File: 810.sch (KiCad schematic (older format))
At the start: 307 parts, among them J1 PJ301BM, J10 PJ301BM, J11 PJ301BM, J12 PJ301BM, J13 PJ301BM, J14 PJ301BM, J15 JACK_MONO_SW, J16 PJ301BM, J17 PJ301B, J18 PJ301B, J2 PJ301BM, J3 PJ301BM, J4 PJ301B, J5 PJ301B, J6 PJ301BM, J7 PJ301BM, J8 PJ301BM, J9 PJ301BM, P1 CONN_01X08, P2 CONN_02X05, P3 CONN_01X03, P4 CONN_01X08, P5 CONN_01X02, Q1 PMBT2369, Q10 2SK208-GR, Q11 2SC4738, Q12 2SA1832, Q13 2SA1832, Q14 2SA1832, Q15 2SC4738, Q2 2SK208-GR, Q3 2SA1618, Q4 2SC4207, Q5 2SK208-GR, Q6 MMBF4391LT1G, Q7 2SA1832, Q8 PMBT2369, Q9 2SK208-GR, SW1 SPDT, SW2 SPDT, SW3 BF3-1050, SW4 SPDT, SW5 DP6T-ALPHA-SR2511, U1 TL072-, U10 TL072-, U11 TL072-, U12 TA75S558F, U13 TA75S558F, U14 TA75S558F, U15 TA75S558F, U16 TA75S558F, U17 CD4052, U18 TA75S558F, U2 TL072-, U3 TL072-, U4 CD40106, U5 CD4027, U6 LM13700, U7 LM13700, U8 LM13700, U9 TL072-

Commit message: added secret sub-oscillator
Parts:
- added C20: 47p, MyModules:SM0603-C-JRL, symbol C_US
- added C47, C48: 0.1µ, MyModules:SM0603-C-JRL, symbol C_US
- added D20, D21, D22: 1N4148, MyModules:SOD323-C1A2, symbol D
- added P6: CONN_02X03, Pin_Headers:Pin_Header_Straight_2x03_Pitch2.54mm, symbol CONN_02X03
- added R143: 220K, MyModules:SM0603-R-JRL, symbol R_US
- added R144: 68K, MyModules:SM0603-R-JRL, symbol R_US
- added R145, R146, R147: 47K, MyModules:SM0603-R-JRL, symbol R_US
- added R148: 100K, MyModules:SM0603-R-JRL, symbol R_US
- added R149: 120K, MyModules:SM0603-R-JRL, symbol R_US
- added R150: 33K, MyModules:SM0603-R-JRL, symbol R_US
- added R5: 10K, MyModules:SM0603-R-JRL, symbol R_US
- added U19: TL072-, MyModules:TSSOP8-JRL, symbol TL072-
- added U20: CD4013, Housings_SSOP:TSSOP-14_4.4x5mm_Pitch0.65mm, symbol 4013
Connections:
- net +10V: now also VR8.3; no longer VR8.1
- net +12V: now also C47.1, R143.2, U19.8 (V+), U20.14 (VDD), U20.14 (VDD)
- net -10V: now also VR8.1; no longer VR8.3
- net -12V: now also C48.2, R144.2, R149.2, U19.4 (V-)
- net GND: now also C47.2, C48.1, R148.1, R5.2, U20.10 (Cd), U20.4 (Cd), U20.6 (Sd), U20.7 (VSS), U20.7 (VSS), U20.8 (Sd)
- net VCO_PULSE: now also U19.3 (+)
- net SUB_OSC: now reaches J3.2
- net SUB_OSC: now also R150.2, U19.7
- new net: D20.1 (K), R144.1, U20.3 (Cp)
- new net: C20.1, R143.1, R5.1, U19.2 (-)
- new net: R145.1, U20.13 (Q)
- new net: D21.2 (A), P6.1 (P1), R145.2
- new net: R146.1, U20.1 (Q), U20.11 (Cp)
- new net: D22.2 (A), P6.5 (P5), R146.2
- new net: U20.2 (~Q), U20.5 (D)
- new net: U20.12 (~Q), U20.9 (D)
- new net: R147.1, R149.1, U19.5 (+)
- new net: R148.2, R150.1, U19.6 (-)
- new net: C20.2, D20.2 (A), U19.1
- new net: P6.2 (P2), P6.4 (P4), P6.6 (P6), R147.2
- new net: D21.1 (K), D22.1 (K), P6.3 (P3)
- no-connect marks 30 -> 29
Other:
- note added: "1_OCT_DOWN_SQUARE"
- note added: "2 OCT DOWN\nPUSLE"
- note added: "2_OCT_DOWN_SQUARE"
- note added: "CLOCK GENERATOR FOR CD4013. \nTHIS WAS TRICKY ON BREADBOARD\nWORKS WITH PULSE BUT NOT TRI."
- note added: "LEVEL SHIFTER"
- note added: "SH101 SUB OSCILLATOR FROM:\nhttp://electro-music.com/forum/topic-18983.html"
- note removed: "REVERSED!"
- moved on the sheet: C27, C28, C29, C30, C31, C32, C34, C35, C37, C38, C39, C40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

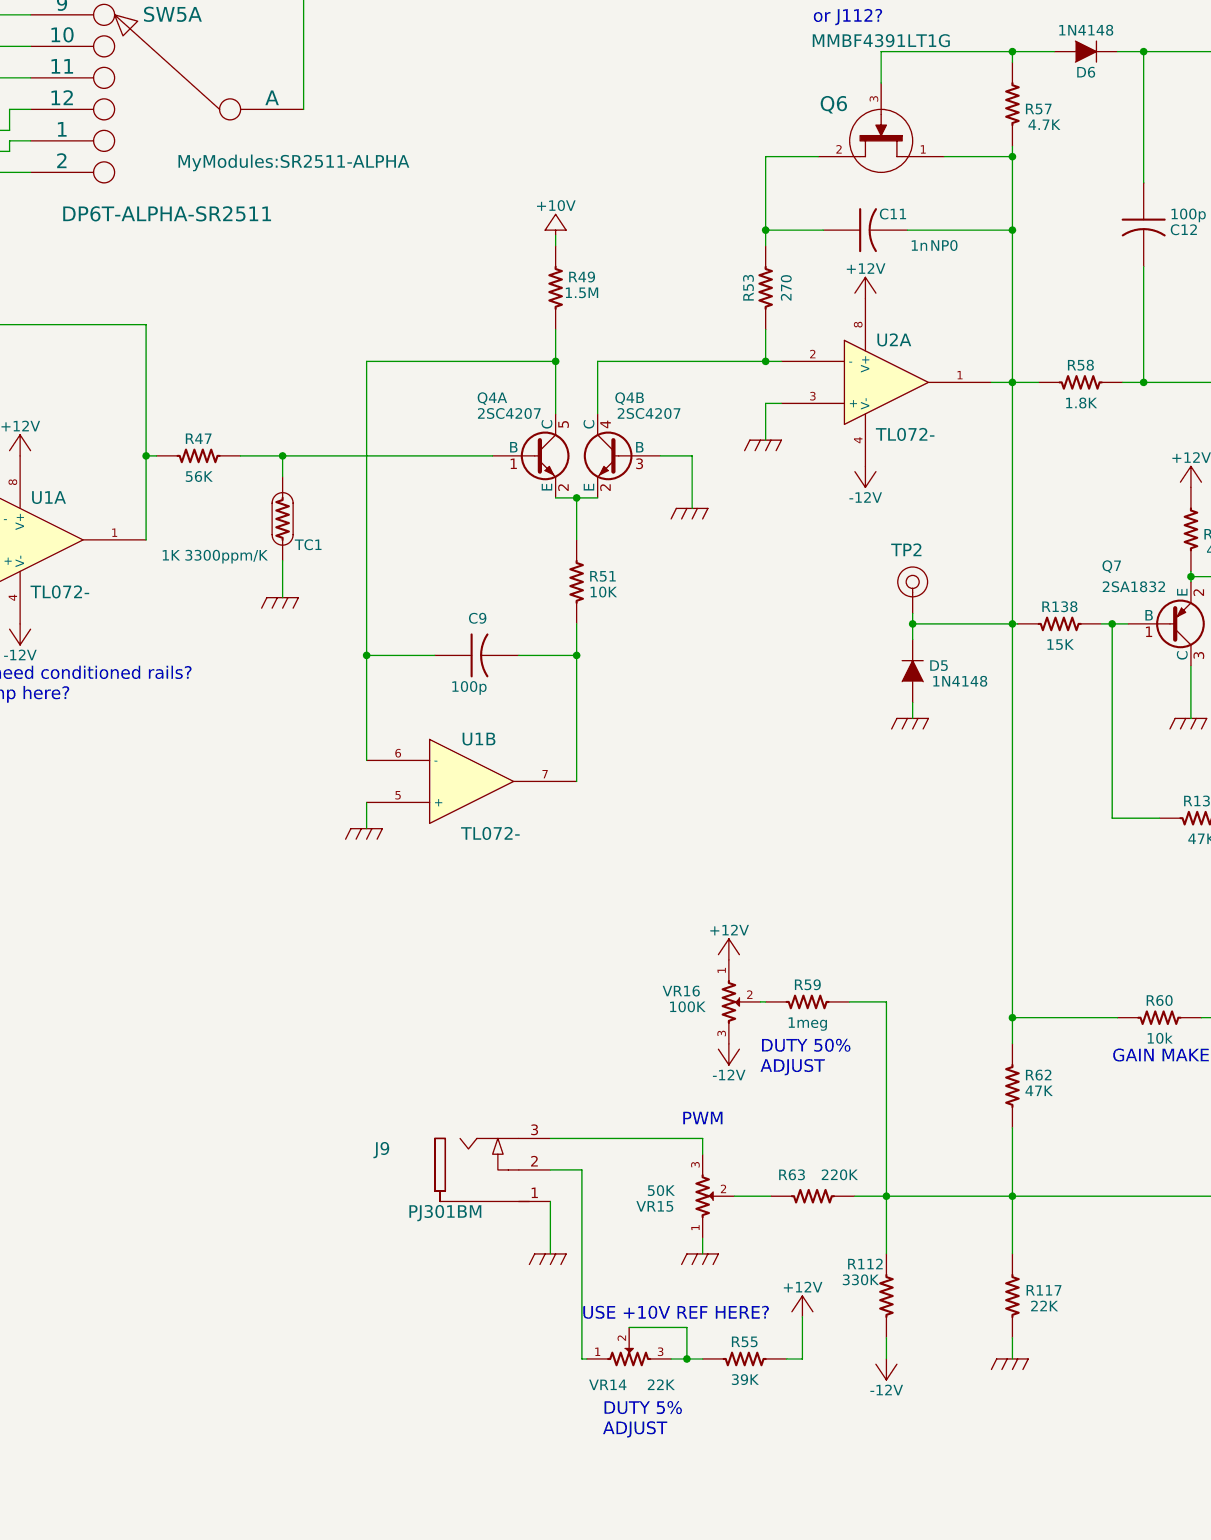
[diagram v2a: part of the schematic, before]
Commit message: couple of changes to schematic to reflect updated part values in r1.1 build
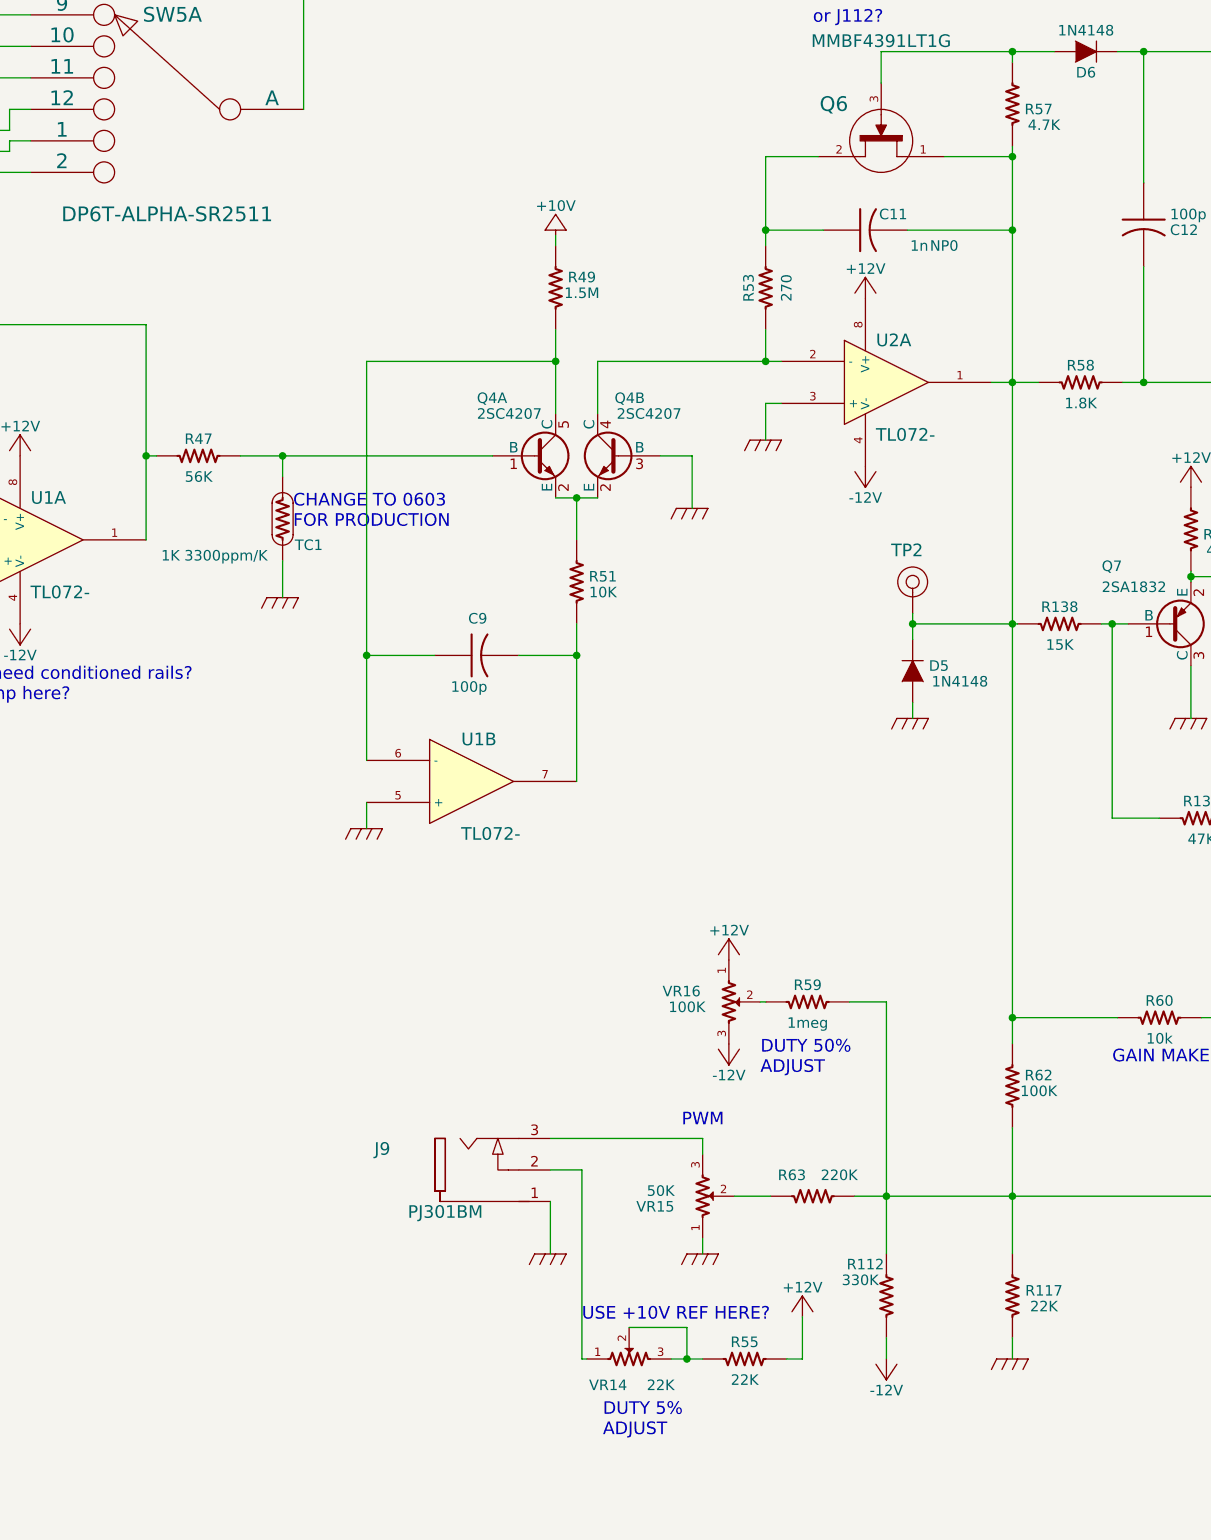
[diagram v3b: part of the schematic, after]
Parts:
- R55: value 39K -> 22K
- R62: value 47K -> 100K
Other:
- note added: "CHANGE TO 0603\nFOR PRODUCTION"
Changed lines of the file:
@@
 P 13150 6675
 F 0 "R62" H 13275 6725 50  0000 C CNN
-F 1 "47K" H 13275 6650 50  0000 C CNN
+F 1 "100K" H 13275 6650 50  0000 C CNN
 F 2 "MyModules:SM0603-R-JRL" H 13150 6675 60  0001 C CNN
 F 3 "" H 13150 6675 60  0001 C CNN
@@
 P 11875 7975
 F 0 "R55" V 11955 7975 50  0000 C CNN
-F 1 "39K" V 11775 7975 50  0000 C CNN
+F 1 "22K" V 11775 7975 50  0000 C CNN
 F 2 "MyModules:SM0603-R-JRL" H 11875 7975 60  0001 C CNN
 F 3 "" H 11875 7975 60  0001 C CNN
@@
 F 0 "SW5" H 9100 2475 70  0000 C CNN
 F 1 "DP6T-ALPHA-SR2511" H 9125 1525 70  0000 C CNN
-F 2 "MyModules:SR2511-ALPHA" H 8525 1775 60  0000 C CNN
+F 2 "MyModules:SR2511-ALPHA" H 8525 1775 60  0001 C CNN
 F 3 "" H 8525 1775 60  0000 C CNN
 	1    9125 2025
@@
 	26425 17400 26425 18400
 Connection ~ 26425 17900
+Text Notes 9725 4025 0    60   ~ 0
+CHANGE TO 0603\nFOR PRODUCTION
 $EndSCHEMATC

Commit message: more notes from v1.1 build. sync reset problem with C14 fixed
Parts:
- C1: value 33p -> 100p
- R105, VR25: value 10K -> 100K
- R127: value 100K -> 180K
- R19: value 100K -> 200K
- R20: value 200K -> 180K
- R32: value 220K -> 150K
- R66, R83: value 15K -> 13K
- R71: value 2.4K -> 2.2K
- R73: value 100K -> 150K
- R8: value 33K -> 100K
- VR10, VR9: value 100K -> 100K(A)
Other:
- note added: "100K?"
- note added: "100R?"
- note added: "8.2V reset point"
- note added: "BALANCE R83 and R66 for TRI SYMMETRY AND OUTPUT OFFSET"
- note added: "CHANGE R15 to 180K"
- note added: "CHANGE R88 to 47K?"
- note added: "DELETE OR\nREDUCE C14"
- note added: "DELETE R89"
- note added: "DELETE TRIMMER?"
- note removed: "18K?"
- note removed: "8V reset point"
- note removed: "CHANGE R15 to 150K"
- note removed: "DELETE THIS"
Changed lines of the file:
@@
 P 15175 2250
 F 0 "R71" V 15255 2250 50  0000 C CNN
-F 1 "2.4K" V 15075 2250 50  0000 C CNN
+F 1 "2.2K" V 15075 2250 50  0000 C CNN
 F 2 "MyModules:SM0603-R-JRL" H 15175 2250 60  0001 C CNN
 F 3 "" H 15175 2250 60  0001 C CNN
@@
 P 14425 3800
 F 0 "R66" H 14300 3825 50  0000 C CNN
-F 1 "15K" H 14275 3900 50  0000 C CNN
+F 1 "13K" H 14275 3900 50  0000 C CNN
 F 2 "MyModules:SM0603-R-JRL" H 14425 3800 60  0001 C CNN
 F 3 "" H 14425 3800 60  0001 C CNN
@@
 P 16325 2650
 F 0 "R83" H 16200 2675 50  0000 C CNN
-F 1 "15K" H 16175 2750 50  0000 C CNN
+F 1 "13K" H 16175 2750 50  0000 C CNN
 F 2 "MyModules:SM0603-R-JRL" H 16325 2650 60  0001 C CNN
 F 3 "" H 16325 2650 60  0001 C CNN
@@
 P 2475 7000
 F 0 "C1" V 2675 6825 50  0000 L CNN
-F 1 "33p" V 2575 6775 50  0000 L CNN
+F 1 "100p" V 2575 6775 50  0000 L CNN
 F 2 "MyModules:SM0603-C-JRL" H 2475 7000 60  0001 C CNN
 F 3 "" H 2475 7000 60  0000 C CNN
@@
 P 2725 7275
 F 0 "R8" H 2625 7250 50  0000 C CNN
-F 1 "33K" H 2600 7325 50  0000 C CNN
+F 1 "100K" H 2600 7325 50  0000 C CNN
 F 2 "MyModules:SM0603-R-JRL" H 2725 7275 60  0001 C CNN
 F 3 "" H 2725 7275 60  0001 C CNN
@@
 P 6050 6250
 F 0 "R32" V 6130 6250 50  0000 C CNN
-F 1 "220K" V 5950 6250 50  0000 C CNN
+F 1 "150K" V 5950 6250 50  0000 C CNN
 F 2 "MyModules:SM0603-R-JRL" H 6050 6250 60  0001 C CNN
 F 3 "" H 6050 6250 60  0001 C CNN
@@
 NPN here is 2SC752-Y
 Text Notes 14600 2125 0    60   ~ 0
-8V reset point
+8.2V reset point
 Text Notes 14650 4000 0    60   ~ 0
 'Ultrafast' switching BJT
@@
 P 5525 3975
 F 0 "VR9" V 5475 3750 50  0000 C CNN
-F 1 "100K" V 5550 3775 50  0000 C CNN
+F 1 "100K(A)" V 5550 3775 50  0000 C CNN
 F 2 "MyModules:RD901F-ALPHA-POT-T18" H 5525 3975 60  0001 C CNN
 F 3 "" H 5525 3975 60  0000 C CNN
@@
 P 5525 4725
 F 0 "VR10" V 5475 4500 50  0000 C CNN
-F 1 "100K" V 5550 4525 50  0000 C CNN
+F 1 "100K(A)" V 5550 4525 50  0000 C CNN
 F 2 "MyModules:RD901F-ALPHA-POT-T18" H 5525 4725 60  0001 C CNN
 F 3 "" H 5525 4725 60  0000 C CNN
@@
 P 5375 15925
 F 0 "R20" V 5455 15925 50  0000 C CNN
-F 1 "200K" V 5295 15925 50  0000 C CNN
+F 1 "180K" V 5295 15925 50  0000 C CNN
 F 2 "MyModules:SM0603-R-JRL" H 5375 15925 60  0001 C CNN
 F 3 "" H 5375 15925 60  0000 C CNN
@@
 P 5375 15125
 F 0 "R19" V 5455 15125 50  0000 C CNN
-F 1 "100K" V 5295 15125 50  0000 C CNN
+F 1 "200K" V 5295 15125 50  0000 C CNN
 F 2 "MyModules:SM0603-R-JRL" H 5375 15125 60  0001 C CNN
 F 3 "" H 5375 15125 60  0000 C CNN
@@
 P 22925 11700
 F 0 "R127" V 23000 11875 50  0000 C CNN
-F 1 "100K" V 22975 11525 50  0000 C CNN
+F 1 "180K" V 22975 11525 50  0000 C CNN
 F 2 "MyModules:SM0603-R-JRL" H 22925 11700 60  0001 C CNN
 F 3 "" H 22925 11700 60  0001 C CNN
@@
 P 15450 16225
 F 0 "R73" V 15530 16225 50  0000 C CNN
-F 1 "100K" V 15350 16225 50  0000 C CNN
+F 1 "150K" V 15350 16225 50  0000 C CNN
 F 2 "MyModules:SM0603-R-JRL" H 15450 16225 60  0001 C CNN
 F 3 "" H 15450 16225 60  0001 C CNN
@@
 P 19000 18400
 F 0 "R105" V 19075 18575 50  0000 C CNN
-F 1 "10K" V 19050 18225 50  0000 C CNN
+F 1 "100K" V 19050 18225 50  0000 C CNN
 F 2 "MyModules:SM0603-R-JRL" H 19000 18400 60  0001 C CNN
 F 3 "" H 19000 18400 60  0001 C CNN
@@
 P 18700 15575
 F 0 "VR25" V 18850 15725 50  0000 C CNN
-F 1 "10K" V 18775 15775 50  0000 C CNN
+F 1 "100K" V 18775 15775 50  0000 C CNN
 F 2 "MyModules:TC33X-2" H 18700 15575 60  0001 C CNN
 F 3 "" H 18700 15575 60  0000 C CNN
@@
 	1    0    0    -1
 $EndComp
-Text Notes 18250 19950 0    60   ~ 0
-DELETE THIS
 $Comp
 L +12V #PWR0178
@@
 Text Notes 14200 4875 0    60   ~ 0
 8.2K
-Text Notes 16925 6900 0    60   ~ 0
-18K?
 Text Notes 16950 5950 0    60   ~ 0
 GAIN MAKE UP HERE?
 Text Notes 16425 3325 0    60   ~ 0
 GAIN MAKE UP HERE?
-Text Notes 13625 6575 0    60   ~ 0
-GAIN MAKE UP HERE?
 Text Notes 15225 15875 0    60   ~ 0
 CHANGE R73 to 150K
@@
 CHANGE R15 to 100K
 Text Notes 22475 11825 0    60   ~ 0
-CHANGE R15 to 150K
+CHANGE R15 to 180K
 Text Notes 18500 18275 0    60   ~ 0
 CHANGE R105 to 100K
@@
 Text Notes 9725 4025 0    60   ~ 0
 CHANGE TO 0603\nFOR PRODUCTION
+Text Notes 15275 5575 2    60   ~ 0
+DELETE TRIMMER?
+Text Notes 16350 2525 0    60   ~ 0
+BALANCE R83 and R66 for TRI SYMMETRY AND OUTPUT OFFSET
+Text Notes 16075 16575 0    60   ~ 0
+CHANGE R88 to 47K?
+Text Notes 14350 3000 0    60   ~ 0
+DELETE OR\nREDUCE C14
+Text Notes 20875 17325 0    60   ~ 0
+100R?
+Text Notes 21350 18275 0    60   ~ 0
+100K?
+Text Notes 5175 6475 0    60   ~ 0
+MULTI-\nTURN
+Text Notes 17425 5250 2    60   ~ 0
+DELETE R89
 $EndSCHEMATC

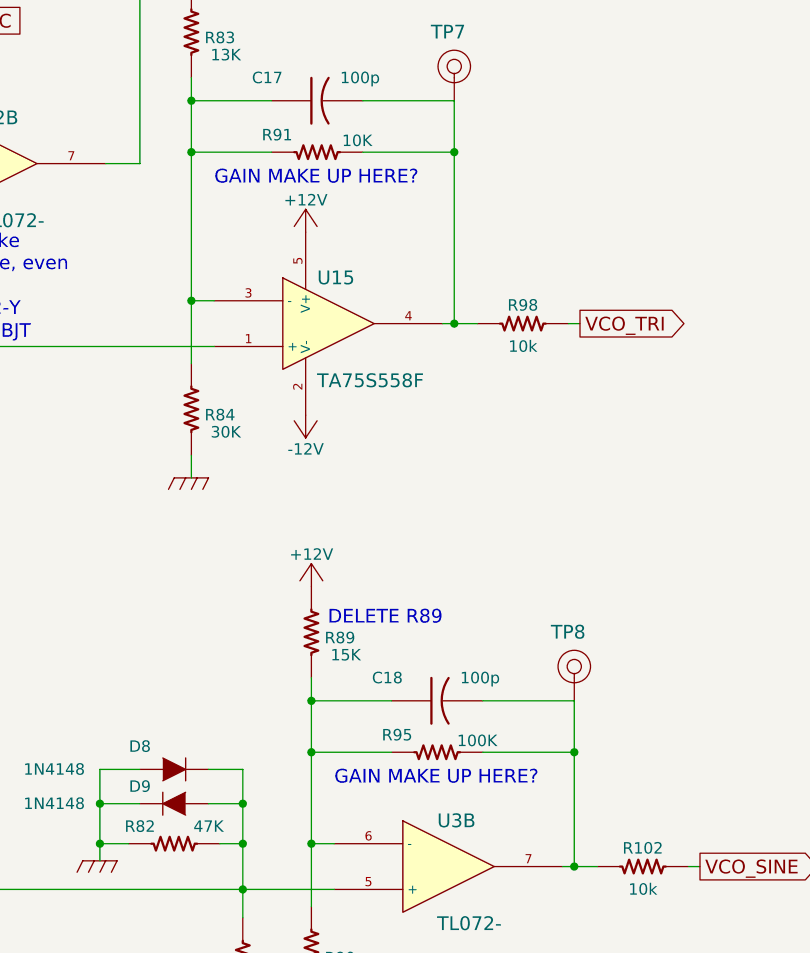
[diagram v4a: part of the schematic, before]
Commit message: ground plane stiching and tweaking
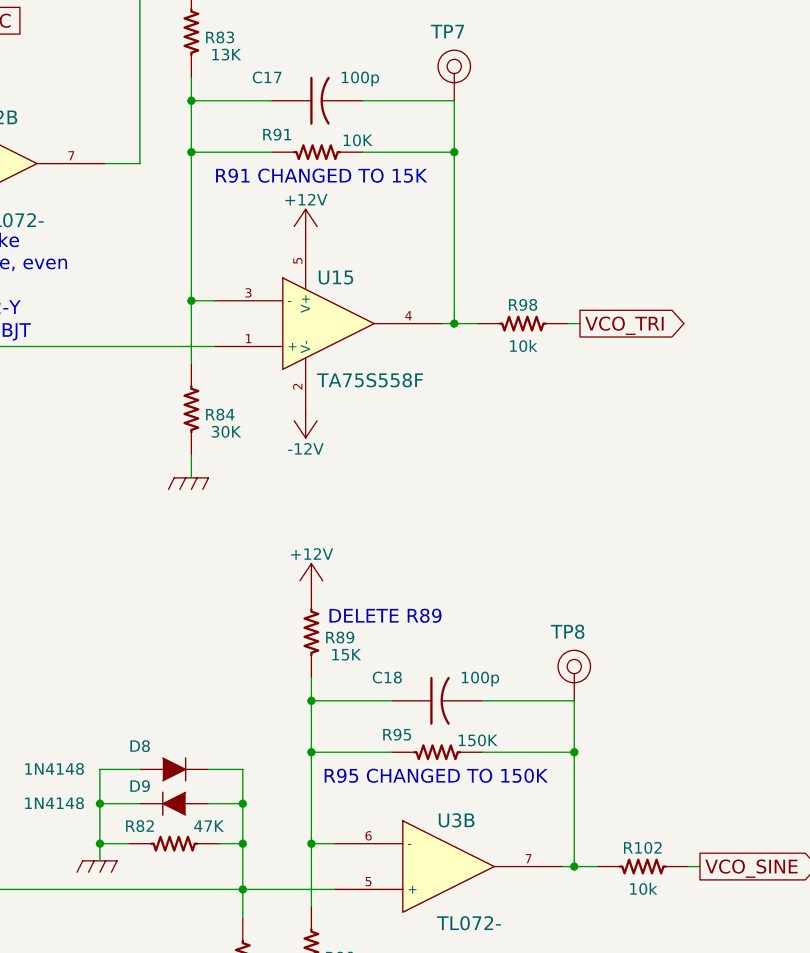
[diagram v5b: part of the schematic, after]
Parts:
- R95: value 100K -> 150K
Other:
- note added: "R91 CHANGED TO 15K"
- note added: "R95 CHANGED TO 150K"
- note removed: "GAIN MAKE UP HERE?"
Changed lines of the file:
@@
 P 17400 5800
 F 0 "R95" V 17475 5975 50  0000 C CNN
-F 1 "100K" V 17450 5625 50  0000 C CNN
+F 1 "150K" V 17450 5625 50  0000 C CNN
 F 2 "MyModules:SM0603-R-JRL" H 17400 5800 60  0001 C CNN
 F 3 "" H 17400 5800 60  0001 C CNN
@@
 Text Notes 14200 4875 0    60   ~ 0
 8.2K
-Text Notes 16950 5950 0    60   ~ 0
-GAIN MAKE UP HERE?
+Text Notes 16900 5950 0    60   ~ 0
+R95 CHANGED TO 150K
 Text Notes 16425 3325 0    60   ~ 0
-GAIN MAKE UP HERE?
+R91 CHANGED TO 15K
 Text Notes 15225 15875 0    60   ~ 0
 CHANGE R73 to 150K
